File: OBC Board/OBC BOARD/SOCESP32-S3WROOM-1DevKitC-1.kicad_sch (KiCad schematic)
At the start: 6 parts, among them IC1 ESP32-S3-WROOM-1-N8R8

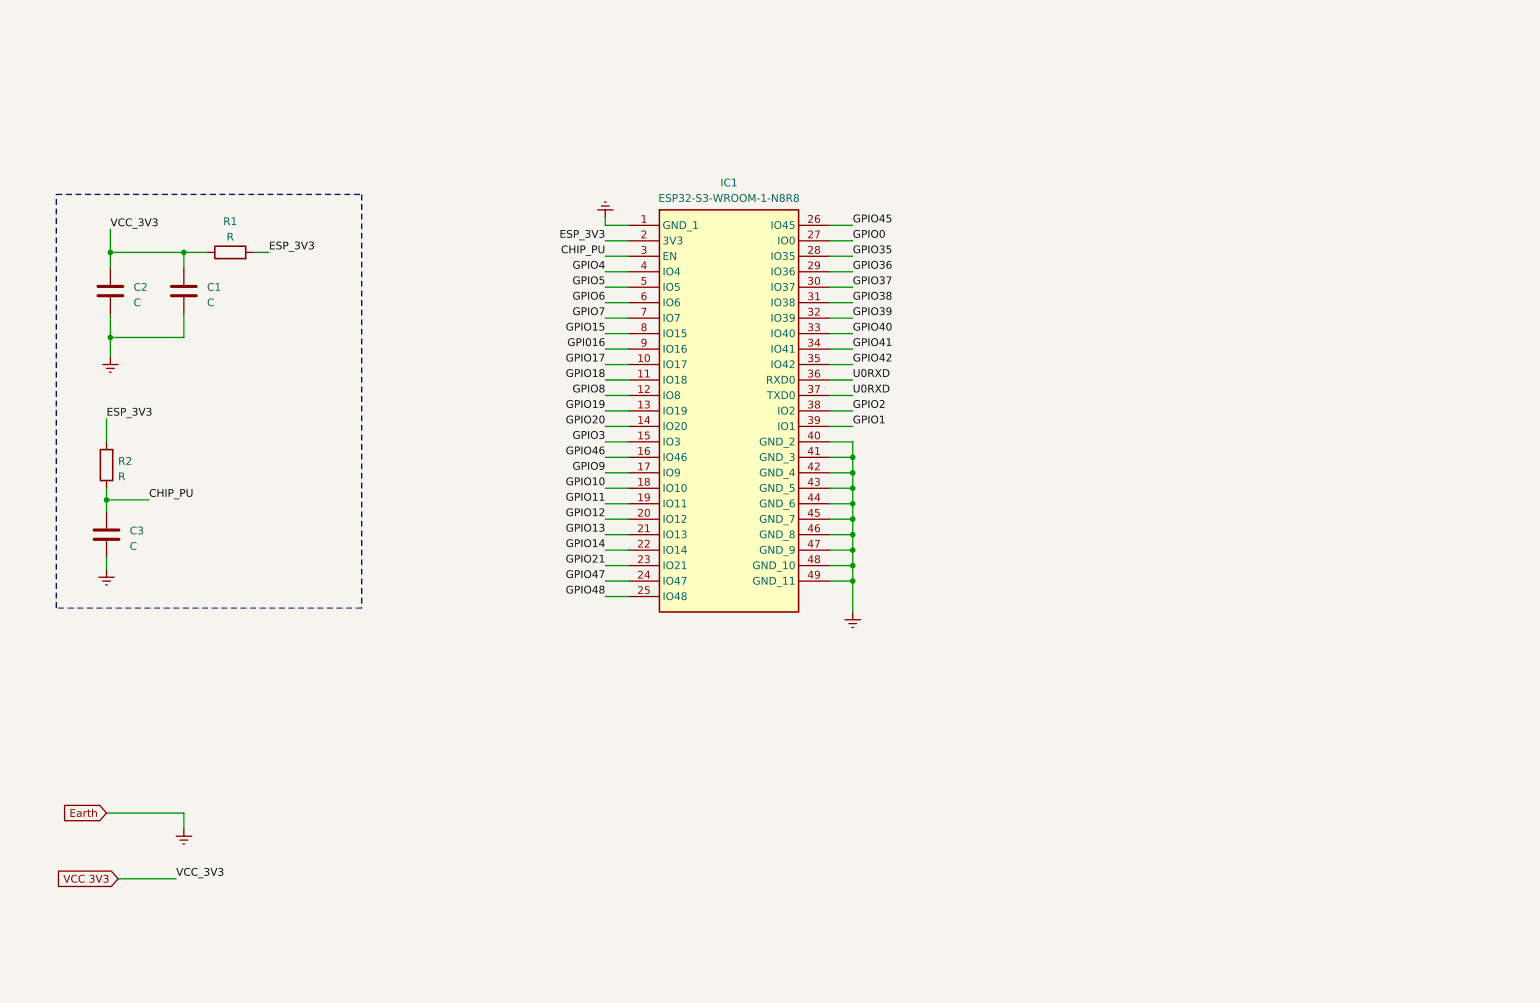
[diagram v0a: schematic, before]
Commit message: Realização do diagrama de blocos, test points, padronização e mudança dos caminhos das bibliotecas de footprints e simbolos
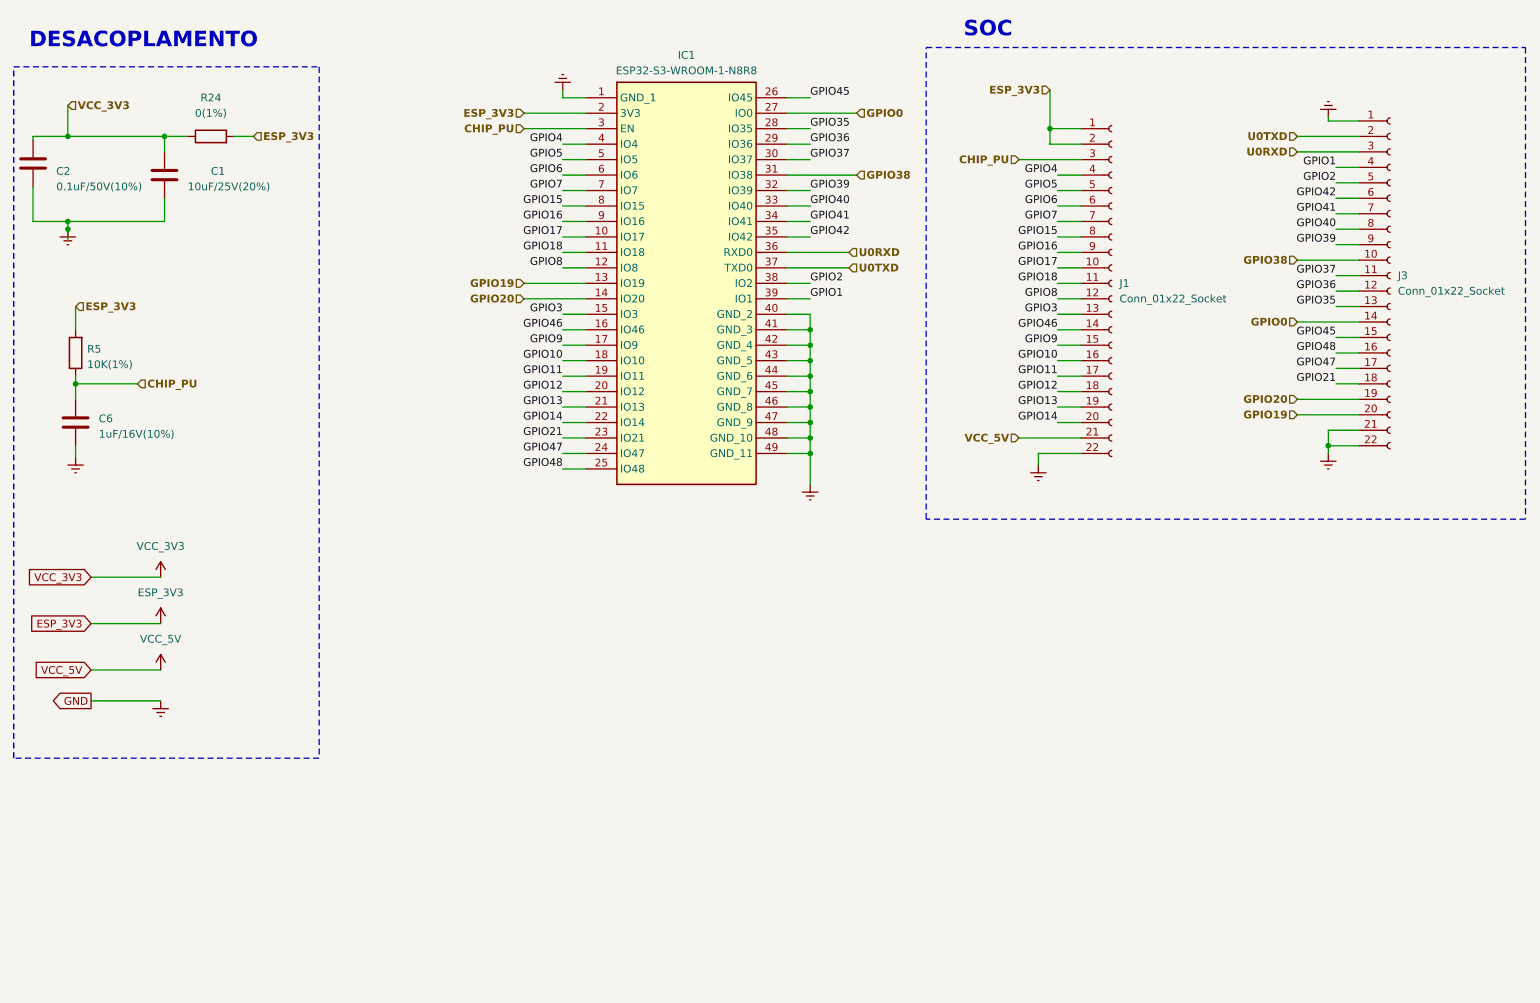
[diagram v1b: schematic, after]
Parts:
- added J1, J3: Conn_01x22_Socket, Connector_PinSocket_2.54mm:PinSocket_1x22_P2.54mm_Vertical, symbol Connector:Conn_01x22_Socket
- C1: value C -> 10uF/25V(20%); footprint (none) -> Capacitor_SMD:C_0402_1005Metric
- C2: value C -> 0.1uF/50V(10%); footprint (none) -> Capacitor_SMD:C_0402_1005Metric
- C6: renamed from C3; value C -> 1uF/16V(10%); footprint (none) -> Capacitor_SMD:C_0402_1005Metric
- IC1: footprint ESP32S3WROOM1N8R8 -> ESP32S3WROOM1N8R8:ESP32S3WROOM1N8R8
- R24: renamed from R1; value R -> 0(1%); footprint (none) -> Resistor_SMD:R_0201_0603Metric
- R5: renamed from R2; value R -> 10K(1%); footprint (none) -> Resistor_SMD:R_0201_0603Metric
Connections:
- net CHIP_PU: now also J1.3 (Pin_3)
- net ESP_3V3: now also J1.1 (Pin_1), J1.2 (Pin_2)
- net Earth: now also J1.22 (Pin_22), J3.1 (Pin_1), J3.21 (Pin_21), J3.22 (Pin_22)
- net GPIO0: now also J3.14 (Pin_14)
- net GPIO1: now also J3.4 (Pin_4)
- net GPIO10: now also J1.16 (Pin_16)
- net GPIO11: now also J1.17 (Pin_17)
- net GPIO12: now also J1.18 (Pin_18)
- net GPIO13: now also J1.19 (Pin_19)
- net GPIO14: now also J1.20 (Pin_20)
- net GPIO15: now also J1.8 (Pin_8)
- net GPIO17: now also J1.10 (Pin_10)
- net GPIO18: now also J1.11 (Pin_11)
- net GPIO19: now also J3.20 (Pin_20)
- net GPIO2: now also J3.5 (Pin_5)
- net GPIO20: now also J3.19 (Pin_19)
- net GPIO21: now also J3.18 (Pin_18)
- net GPIO3: now also J1.13 (Pin_13)
- net GPIO35: now also J3.13 (Pin_13)
- net GPIO36: now also J3.12 (Pin_12)
- net GPIO37: now also J3.11 (Pin_11)
- net GPIO38: now also J3.10 (Pin_10)
- net GPIO39: now also J3.9 (Pin_9)
- net GPIO4: now also J1.4 (Pin_4)
- net GPIO40: now also J3.8 (Pin_8)
- net GPIO41: now also J3.7 (Pin_7)
- net GPIO42: now also J3.6 (Pin_6)
- net GPIO45: now also J3.15 (Pin_15)
- net GPIO46: now also J1.14 (Pin_14)
- net GPIO47: now also J3.17 (Pin_17)
- net GPIO48: now also J3.16 (Pin_16)
- net GPIO5: now also J1.5 (Pin_5)
- net GPIO6: now also J1.6 (Pin_6)
- net GPIO7: now also J1.7 (Pin_7)
- net GPIO8: now also J1.12 (Pin_12)
- net GPIO9: now also J1.15 (Pin_15)
- net U0RXD: now also J3.3 (Pin_3); no longer IC1.37 (TXD0)
- net GPI016 renamed GPIO16
- net GPIO16: now also J1.9 (Pin_9)
- net VCC 3V3 renamed VCC_3V3
- new net U0TXD: IC1.37 (TXD0), J3.2 (Pin_2)
- new net VCC_5V: J1.21 (Pin_21)
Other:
- note added: "DESACOPLAMENTO"
- note added: "SOC"
- title: ICARUS-2 OBCH -> ICARUS-2 OBDH
- moved on the sheet: C1, C2, C6, IC1, R24, R5

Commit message: Junção dos projetos FPGA e ESP32. Biblioteca de simbolos e footprints realizadas. Definição do caminho para os arquivos. Inclusão do esquema librecube.
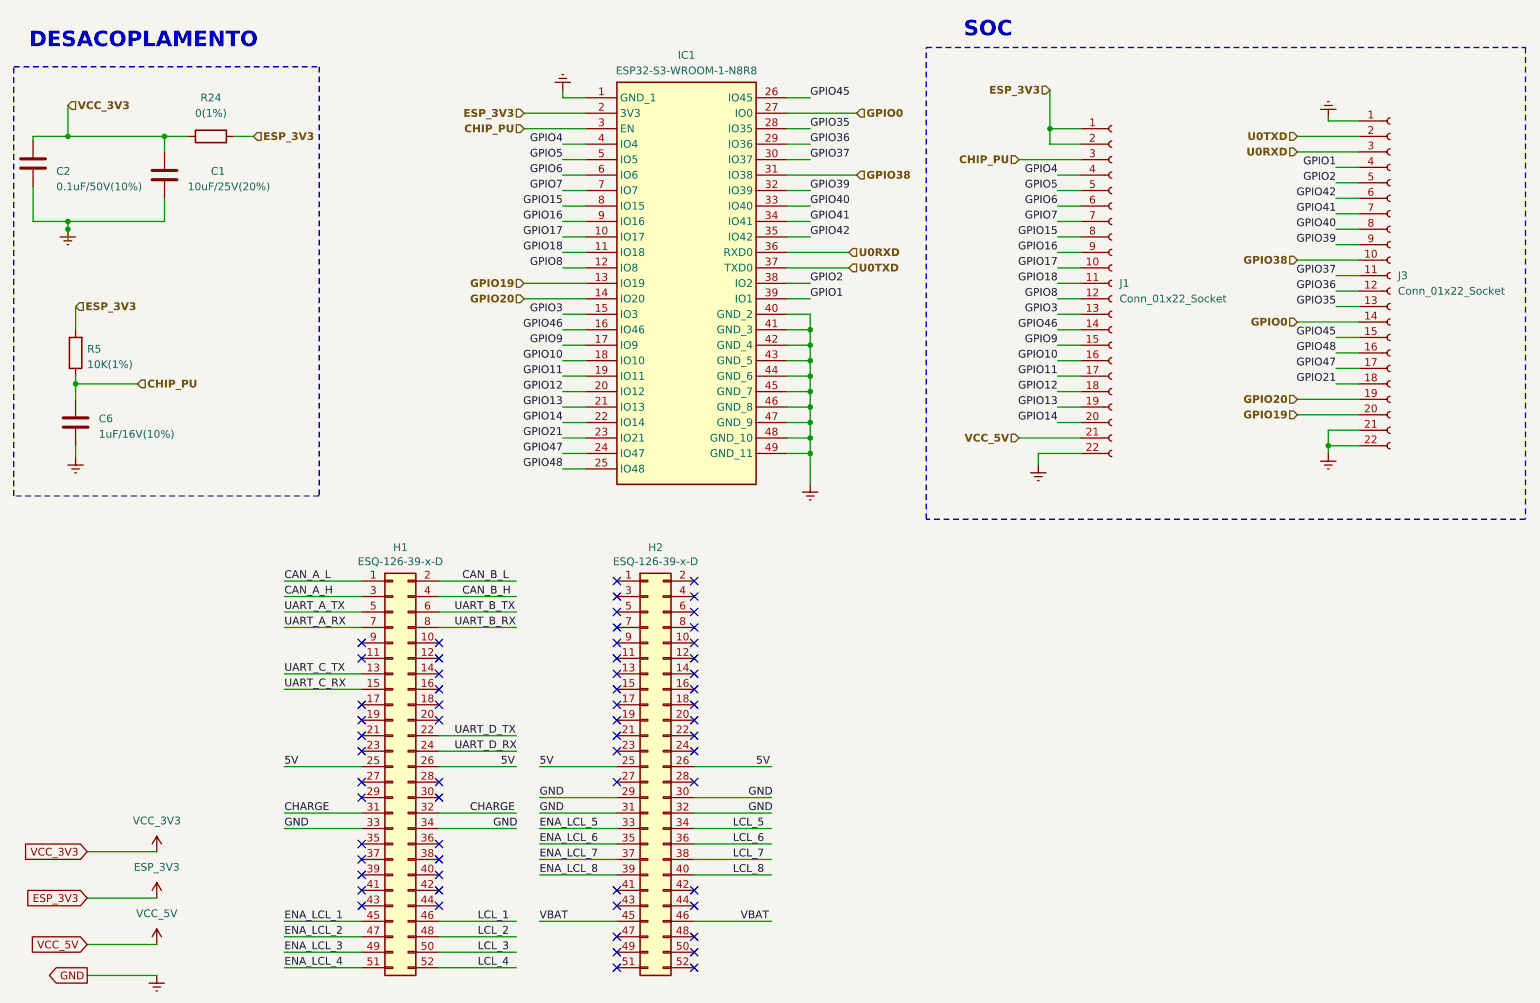
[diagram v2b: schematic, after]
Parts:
- added H1, H2: ESQ-126-39-x-D, Connector_PinHeader_2.54mm:PinHeader_2x26_P2.54mm_Vertical, symbol Connector_Generic:Conn_02x26_Odd_Even
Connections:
- net Earth: now also H1.33 (Pin_33), H1.34 (Pin_34), H2.29 (Pin_29), H2.30 (Pin_30), H2.31 (Pin_31), H2.32 (Pin_32)
- new net 5V: H1.25 (Pin_25), H1.26 (Pin_26), H2.25 (Pin_25), H2.26 (Pin_26)
- new net CAN_A_H: H1.3 (Pin_3)
- new net CAN_A_L: H1.1 (Pin_1)
- new net CAN_B_H: H1.4 (Pin_4)
- new net CAN_B_L: H1.2 (Pin_2)
- new net CHARGE: H1.31 (Pin_31), H1.32 (Pin_32)
- new net ENA_LCL_1: H1.45 (Pin_45)
- new net ENA_LCL_2: H1.47 (Pin_47)
- new net ENA_LCL_3: H1.49 (Pin_49)
- new net ENA_LCL_4: H1.51 (Pin_51)
- new net ENA_LCL_5: H2.33 (Pin_33)
- new net ENA_LCL_6: H2.35 (Pin_35)
- new net ENA_LCL_7: H2.37 (Pin_37)
- new net ENA_LCL_8: H2.39 (Pin_39)
- new net LCL_1: H1.46 (Pin_46)
- new net LCL_2: H1.48 (Pin_48)
- new net LCL_3: H1.50 (Pin_50)
- new net LCL_4: H1.52 (Pin_52)
- new net LCL_5: H2.34 (Pin_34)
- new net LCL_6: H2.36 (Pin_36)
- new net LCL_7: H2.38 (Pin_38)
- new net LCL_8: H2.40 (Pin_40)
- new net UART_A_RX: H1.7 (Pin_7)
- new net UART_A_TX: H1.5 (Pin_5)
- new net UART_B_RX: H1.8 (Pin_8)
- new net UART_B_TX: H1.6 (Pin_6)
- new net UART_C_RX: H1.15 (Pin_15)
- new net UART_C_TX: H1.13 (Pin_13)
- new net UART_D_RX: H1.24 (Pin_24)
- new net UART_D_TX: H1.22 (Pin_22)
- new net VBAT: H2.45 (Pin_45), H2.46 (Pin_46)
- no-connect marks 0 -> 62
